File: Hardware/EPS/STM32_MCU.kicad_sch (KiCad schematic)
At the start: 32 parts, among them J201 Conn_ARM_JTAG_SWD_10, U201 STM32L431RCT, U202 HZ0805E601R-10

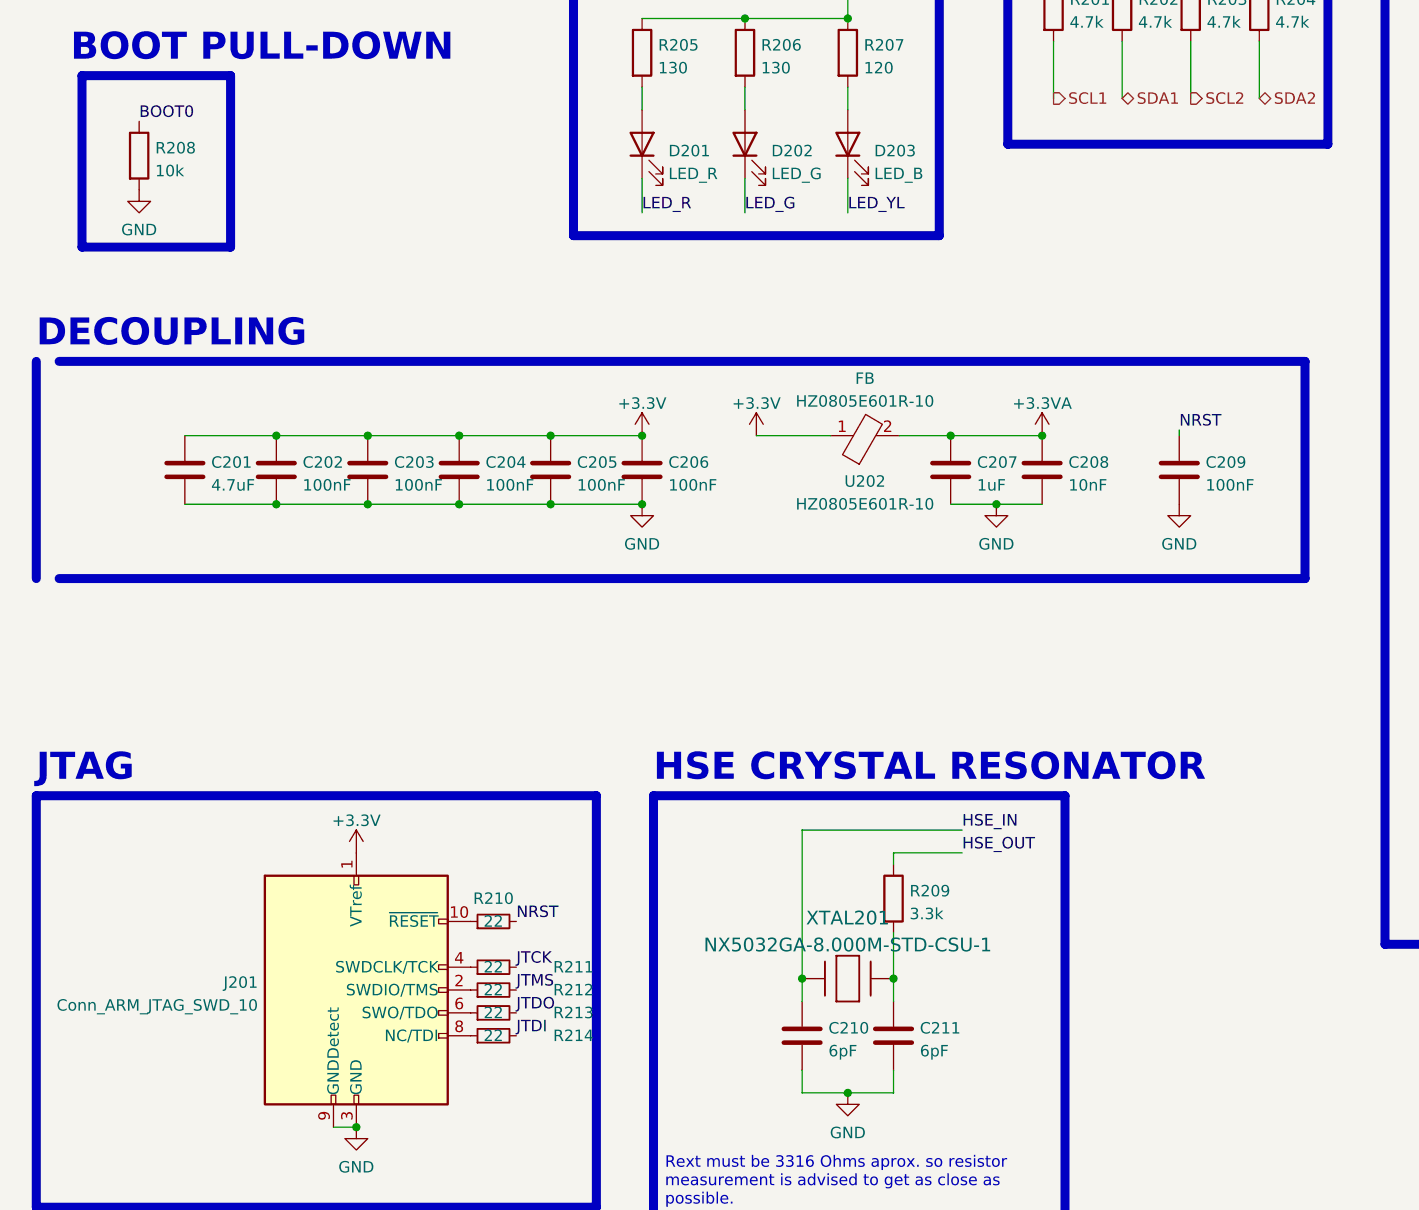
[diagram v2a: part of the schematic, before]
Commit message: Updated to KiCAD 7.0
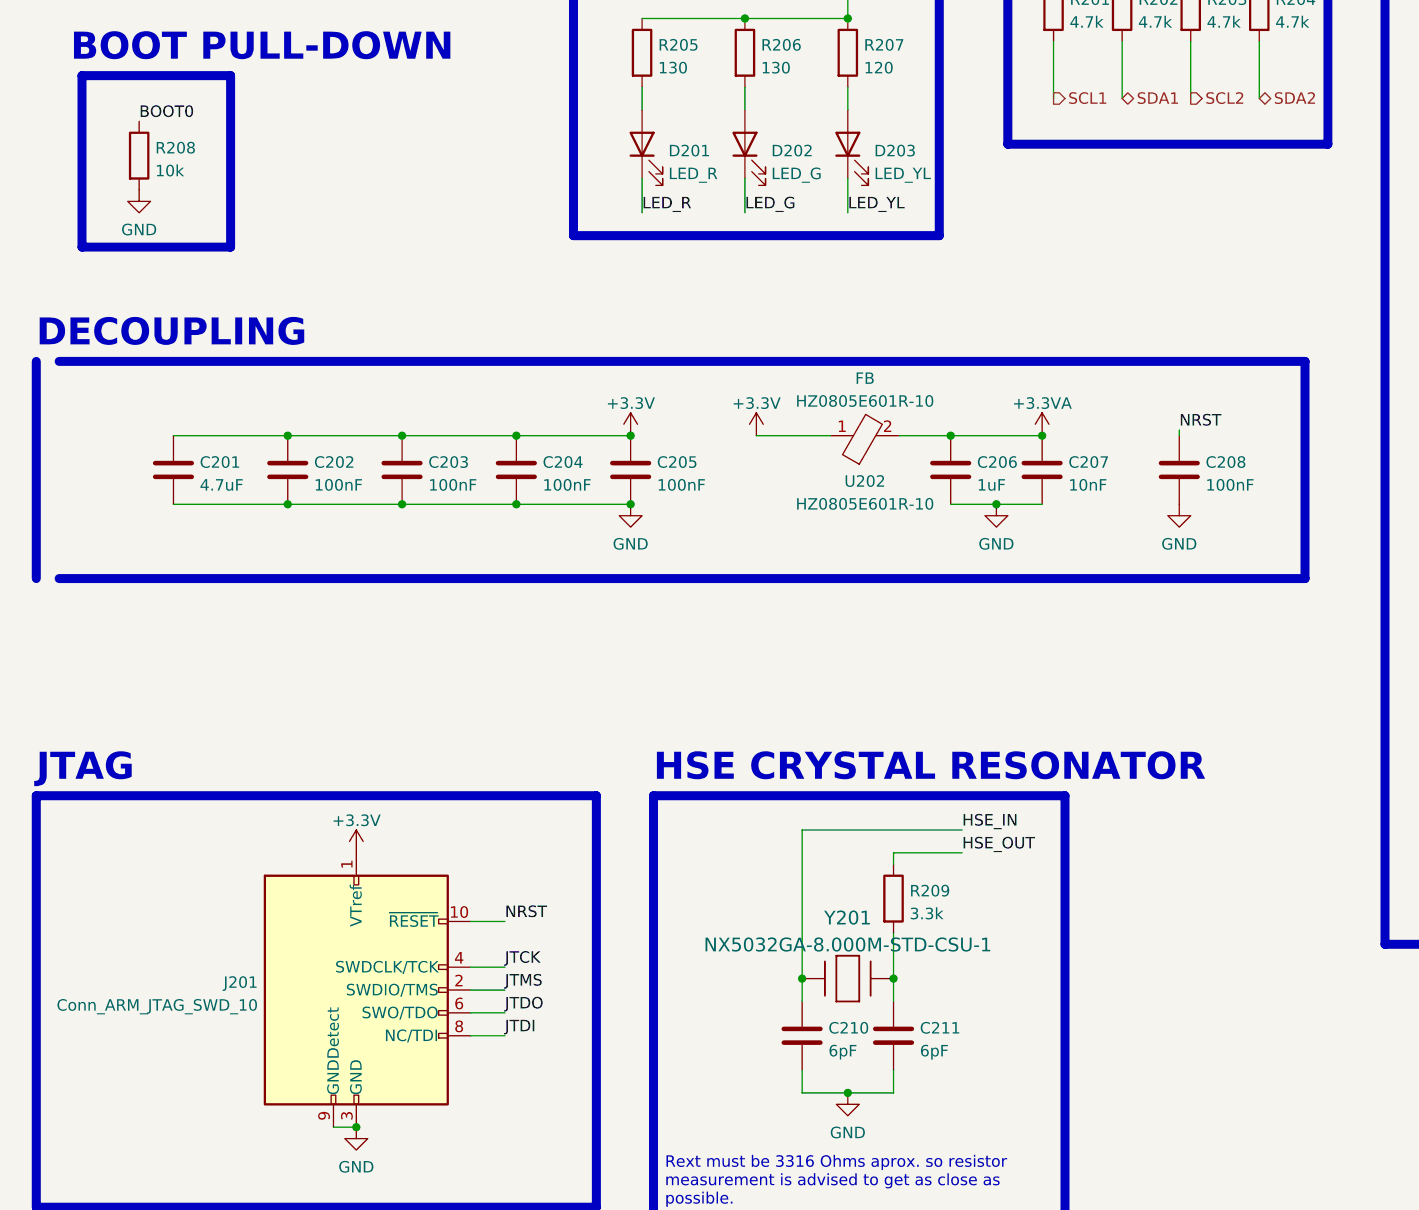
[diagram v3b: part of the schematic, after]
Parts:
- removed C202: 100nF, Capacitor_SMD:C_0603_1608Metric_Pad1.08x0.95mm_HandSolder, symbol Device:C
- removed R210, R211, R212, R213, R214: 22, Resistor_SMD:R_0603_1608Metric_Pad0.98x0.95mm_HandSolder, symbol Device:R_Small
- D203: value LED_B -> LED_YL
- J201: footprint digikey-footprints:PinHeader_2x5_P1.27mm_Drill.7mm -> Connector_PinHeader_2.00mm:PinHeader_2x05_P2.00mm_Vertical
- renumbered C203 to C202, C204 to C203, C205 to C204, C206 to C205, C207 to C206, C208 to C207, C209 to C208, XTAL201 to Y201
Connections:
- net JTCK: now also J201.4 (SWDCLK/TCK)
- net JTDI: now also J201.8 (NC/TDI)
- net JTDO: now also J201.6 (SWO/TDO)
- net JTMS: now also J201.2 (SWDIO/TMS)
- net NRST: now also J201.10 (~{RESET})
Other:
- moved on the sheet: C201, C202, C203, C204, C205
